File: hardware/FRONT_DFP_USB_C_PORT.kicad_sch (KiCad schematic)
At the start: 26 parts, among them J5 USB4200-03-A (VIRT FLAG MOUNT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, Q18 PMOS, Q19 PMOS, Q20 PMOS, Q21 PMOS

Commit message: finnished rudimentry schimatics still needs alot of work
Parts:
- removed D11 (x2): ~, symbol CARTHING:PUSB3FR6
- removed U12: ~, symbol CARTHING:USB5916C
- added D11 (x2): ~, symbol CARTHING:PUSB3FR6
- added U12: ~, symbol CARTHING:USB5916C
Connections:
- net +3V3: no longer U14.14 (SLV_ADDR)
- net GND: now also U14.14 (SLV_ADDR), D11.2 (GND), D11.2 (GND)
- net B_USB-C_BUCK_OUT renamed F_USB-C_BUCK_OUT
- net UFP_2_N renamed DFP_2_N
- net DFP_2_N: now also D11.3 (CH2), U12.7 (USB2DN_DM1/PRT_DIS_M1)
- net UFP_2_P renamed DFP_2_P
- net DFP_2_P: now also D11.1 (CH1), U12.6 (USB2DN_DP1/PRT_DIS_P1)
- net UFP_3_RXA_N renamed DFP_3_RXA_N
- net DFP_3_RXA_N: now also D11.7 (CH6), U12.12 (USB3DN_RXDM1A)
- net UFP_3_RXA_P renamed DFP_3_RXA_P
- net DFP_3_RXA_P: now also D11.6 (CH5), U12.11 (USB3DN_RXDP1A)
- net UFP_3_RXB_N renamed DFP_3_RXB_N
- net DFP_3_RXB_N: now also D11.4 (CH3), U12.19 (USB3DN_RXDM1B)
- net UFP_3_RXB_P renamed DFP_3_RXB_P
- net DFP_3_RXB_P: now also D11.5 (CH4), U12.18 (USB3DN_RXDP1B)
- net UFP_3_TXA_N renamed DFP_3_TXA_N
- net DFP_3_TXA_N: now also D11.5 (CH4)
- net UFP_3_TXA_P renamed DFP_3_TXA_P
- net DFP_3_TXA_P: now also D11.4 (CH3)
- net UFP_3_TXB_N renamed DFP_3_TXB_N
- net DFP_3_TXB_N: now also D11.1 (CH1), U12.16 (USB3DN_TXDM1B)
- net UFP_3_TXB_P renamed DFP_3_TXB_P
- net DFP_3_TXB_P: now also D11.3 (CH2), U12.15 (USB3DN_TXDP1B)
- net UFP_CC1 renamed DFP_CC1
- net DFP_CC1: now also D11.6 (CH5)
- net UFP_CC2 renamed DFP_CC2
- net DFP_CC2: now also D11.7 (CH6)
- net UFP_CC_CTRL renamed DFP_CC_CTRL
- net UFP_CC_ORIENT renamed DFP_CC_ORIENT
- net DFP_CC_ORIENT: now also U12.50 (AB1/ATTACHMUX1B/GPIO65)
- net UFP_PD_INT renamed DFP_PD_INT
- net UFP_VBUS renamed DFP_VBUS
- new net DFP_C_ATTACH_1: U12.76 (C_ATTACH1/ATTACHMUX1A/GPIO1)
- no-connect marks 4 -> 5
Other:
- note added: "ADDR 0XE0"
- note added: "PMPB27EP"
- note removed: "ADDR 0XE4"

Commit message: working on hardware
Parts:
- added C100 (x2), C99 (x2): 0.1uF, Capacitor_SMD:C_0603_1608Metric, symbol Device:C
- C80, C81, C82, C83, C84, C85: footprint (none) -> Capacitor_SMD:C_0603_1608Metric
- JP1, JP2, JP5, JP6, JP7: footprint (none) -> Jumper:SolderJumper-3_P1.3mm_Open_RoundedPad1.0x1.5mm_NumberLabels
- Q18, Q19, Q20, Q21: footprint (none) -> CARTHING:TRANS_PMPB11EN_115
- TP1: footprint (none) -> TestPoint:TestPoint_Pad_D1.5mm
- renumbered U12 to U13
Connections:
- net DFP_3_RXB_N: now also C99.2; no longer J5.B10 (RX1-)
- net DFP_3_RXB_P: now also C100.1; no longer J5.B11 (RX1+)
- net DFP_3_TXB_N: now also C99.2; no longer J5.B3 (TX2-)
- net DFP_3_TXB_P: now also C100.1; no longer J5.B2 (TX2+)
- new net: C100.2, J5.B11 (RX1+)
- new net: C99.1, J5.B10 (RX1-)
- new net: C100.2, J5.B2 (TX2+)
- new net: C99.1, J5.B3 (TX2-)
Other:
- note added: "EHUB CHIP DFP BLOCK"
- note added: "ESD PROTECTION"
- note added: "FRONT USB-C PORT CONTROLER"
- note added: "PHISICAL USB-C DOWNSTREAM PORT"
- moved on the sheet: C80, C81, C82, C83, C84, C85, D11, JP1, JP2, JP5, JP6, JP7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

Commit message: working assighning footprints still
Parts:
- R89, R90, R91, R92, R93: footprint (none) -> Resistor_SMD:R_0603_1608Metric
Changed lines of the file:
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@@
       (effects (font (size 1.27 1.27)) (justify left))
     )
-    (property "Footprint" "" (at 193.802 144.78 90)
+    (property "Footprint" "Resistor_SMD:R_0603_1608Metric" (at 193.802 144.78 90)
       (effects (font (size 1.27 1.27)) hide)
     )
@@
       (effects (font (size 1.27 1.27)))
     )
-    (property "Footprint" "" (at 177.8 128.778 90)
+    (property "Footprint" "Resistor_SMD:R_0603_1608Metric" (at 177.8 128.778 90)
       (effects (font (size 1.27 1.27)) hide)
     )
@@
       (effects (font (size 1.27 1.27)) (justify left))
     )
-    (property "Footprint" "" (at 73.152 170.18 90)
+    (property "Footprint" "Resistor_SMD:R_0603_1608Metric" (at 73.152 170.18 90)
       (effects (font (size 1.27 1.27)) hide)
     )
@@
       (effects (font (size 1.27 1.27)))
     )
-    (property "Footprint" "" (at 177.8 154.178 90)
+    (property "Footprint" "Resistor_SMD:R_0603_1608Metric" (at 177.8 154.178 90)
       (effects (font (size 1.27 1.27)) hide)
     )
@@
       (effects (font (size 1.27 1.27)) (justify left))
     )
-    (property "Footprint" "" (at 193.802 119.38 90)
-      (effects (font (size 1.27 1.27)) hide)
-    )
+    (property "Footprint" "Resistor_SMD:R_0603_1608Metric" (at 193.802 119.38 90)
+      (effects (font (size 1.27 1.27)) hide)
+    )

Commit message: FINALY starting the pcb
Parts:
- D11: footprint (none) -> CARTHING:PUSB3AB6Z_NEX
- J5: footprint (none) -> CARTHING:USB4200-03-A_REVA
- U13: footprint (none) -> CARTHING:VQFN100_KD_MCH
- U14: footprint (none) -> CARTHING:PTN5100BSMP
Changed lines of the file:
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@@
       (effects (font (size 1.27 1.27)))
     )
-    (property "Footprint" "" (at 44.45 54.61 0)
+    (property "Footprint" "CARTHING:USB4200-03-A_REVA" (at 44.45 54.61 0)
       (effects (font (size 1.27 1.27)) hide)
     )
@@
       (effects (font (size 1.27 1.27)))
     )
-    (property "Footprint" "" (at 138.43 25.4 0)
+    (property "Footprint" "CARTHING:PUSB3AB6Z_NEX" (at 138.43 25.4 0)
       (effects (font (size 1.27 1.27)) hide)
     )
@@
       (effects (font (size 1.27 1.27)))
     )
-    (property "Footprint" "" (at 241.3 87.63 0)
+    (property "Footprint" "CARTHING:VQFN100_KD_MCH" (at 241.3 87.63 0)
       (effects (font (size 1.27 1.27)) hide)
     )
@@
       (effects (font (size 1.27 1.27)))
     )
-    (property "Footprint" "" (at 138.43 53.34 0)
+    (property "Footprint" "CARTHING:PUSB3AB6Z_NEX" (at 138.43 53.34 0)
       (effects (font (size 1.27 1.27)) hide)
     )
@@
       (effects (font (size 1.27 1.27)))
     )
-    (property "Footprint" "" (at 102.87 127 0)
-      (effects (font (size 1.27 1.27)) hide)
-    )
+    (property "Footprint" "CARTHING:PTN5100BSMP" (at 102.87 127 0)
+      (effects (font (size 1.27 1.27)) hide)
+    )

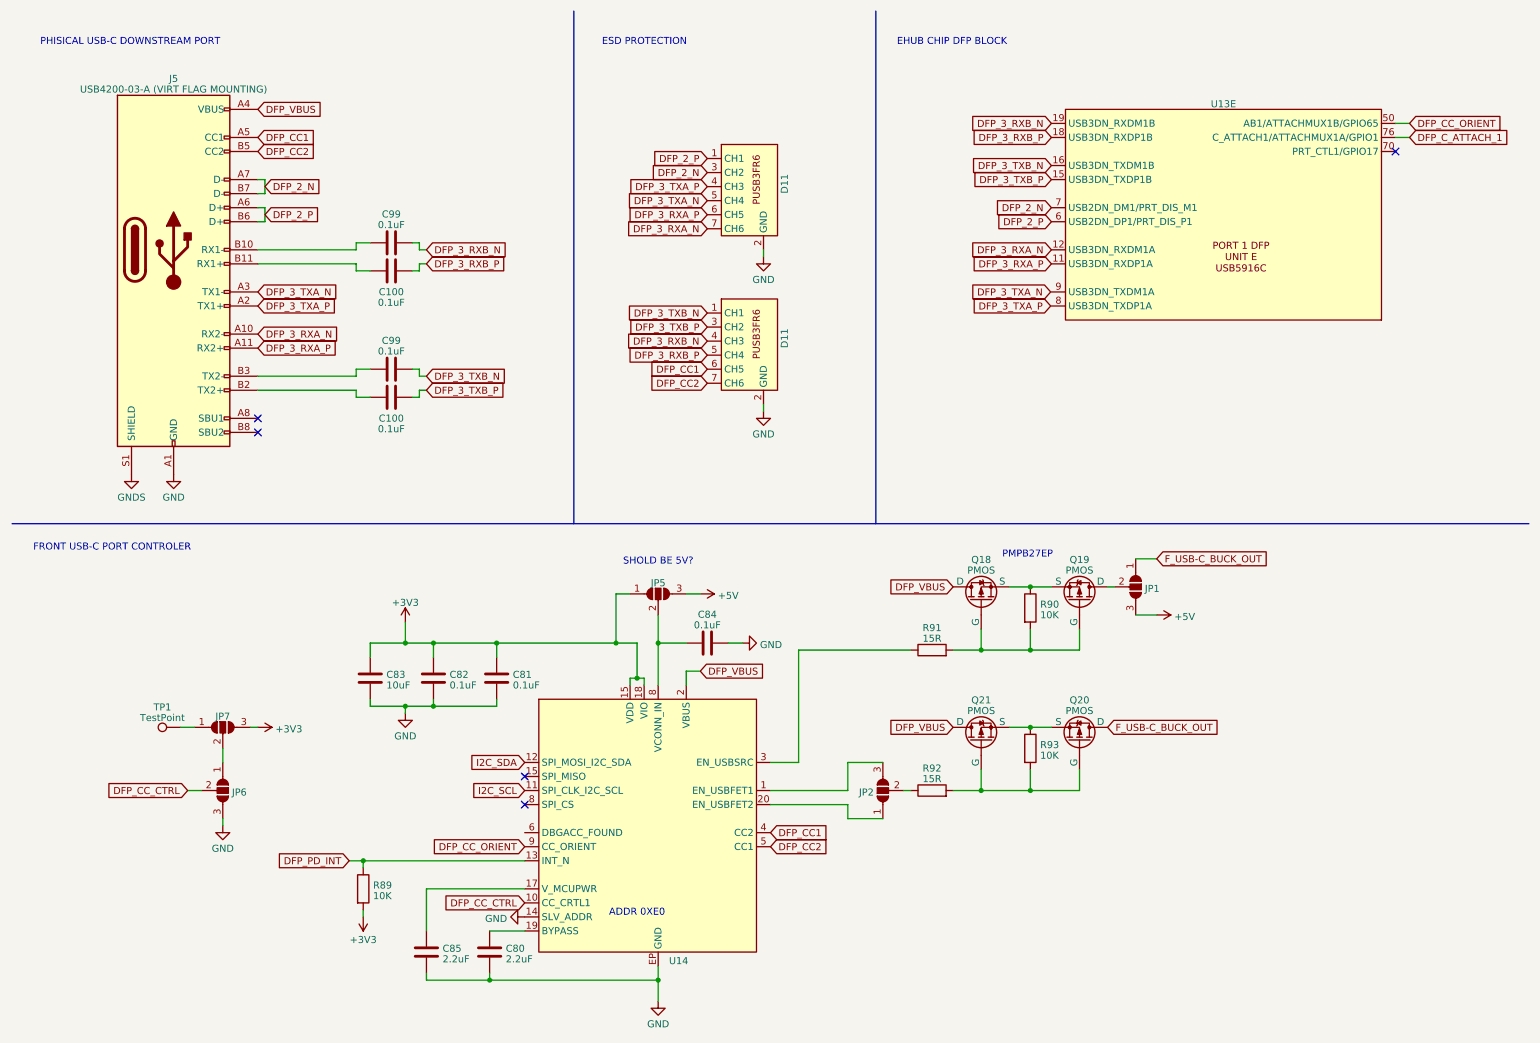
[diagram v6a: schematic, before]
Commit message: worked on usb port and display routing
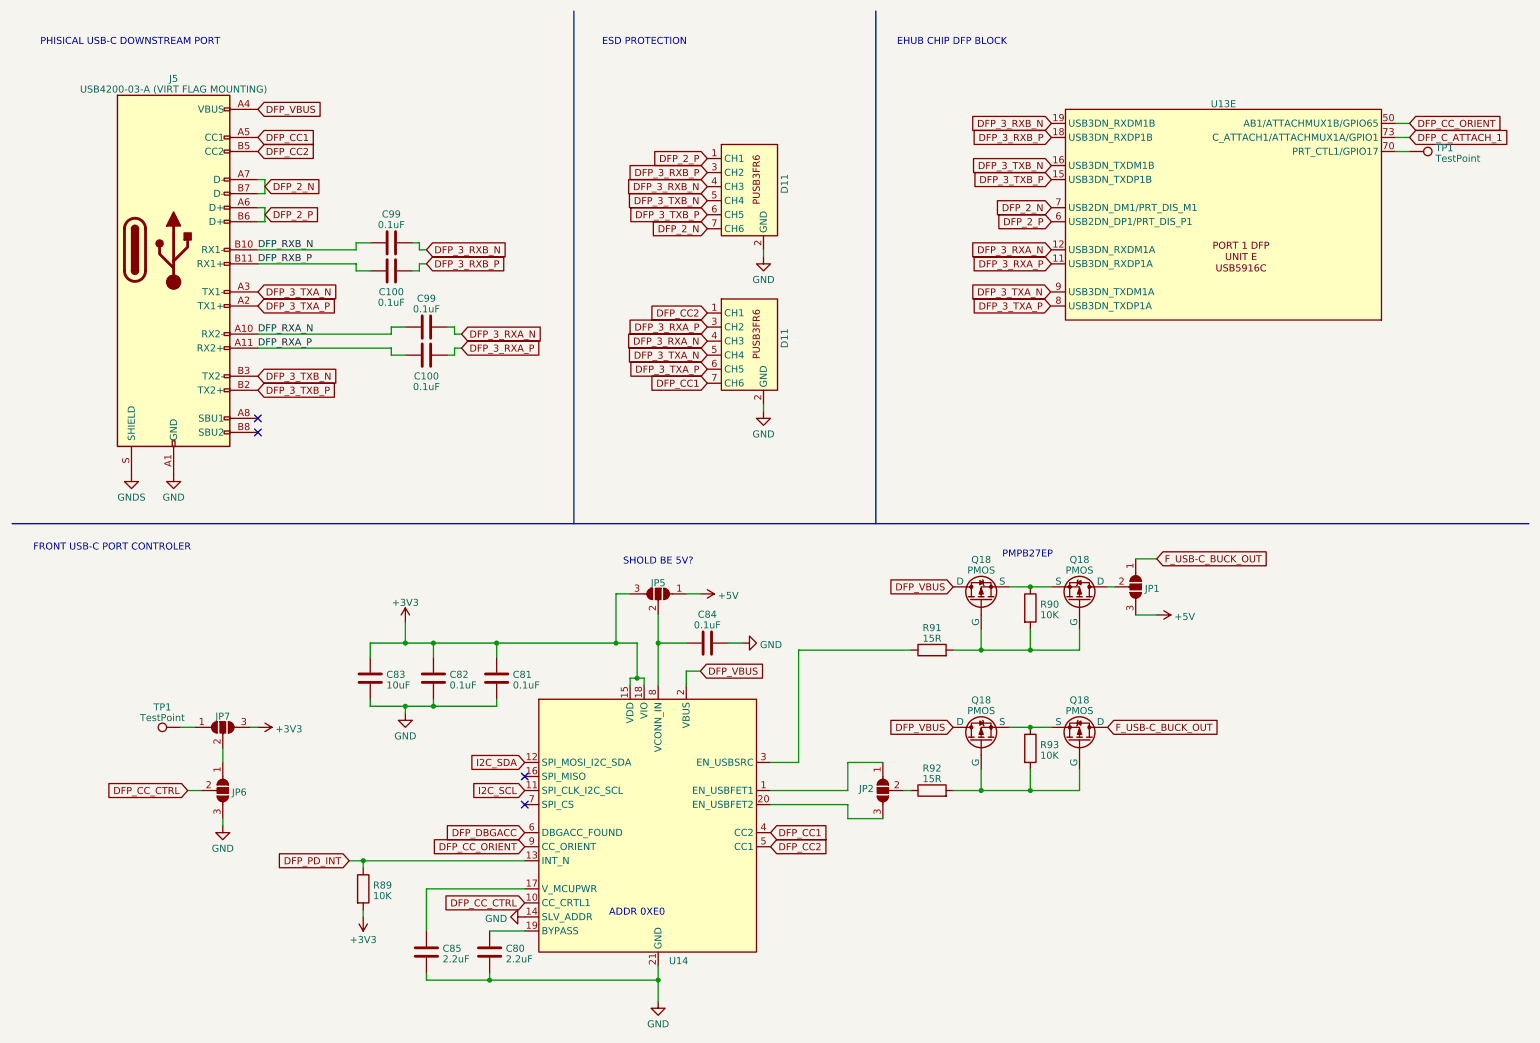
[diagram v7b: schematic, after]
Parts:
- removed Q19, Q20, Q21: PMOS, CARTHING:TRANS_PMPB11EN_115, symbol Simulation_SPICE:PMOS
- added Q18 (x3): PMOS, CARTHING:TRANS_PMPB11EN_115, symbol Simulation_SPICE:PMOS
- added TP1: TestPoint, TestPoint:TestPoint_Pad_D1.5mm, symbol Connector:TestPoint
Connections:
- net +3V3: now also JP5.3 (B); no longer JP5.1 (A)
- net +5V: now also JP5.1 (A); no longer JP5.3 (B)
- net DFP_2_N: now also D11.7 (CH6); no longer D11.3 (CH2)
- net DFP_3_RXA_N: now also C99.2, D11.4 (CH3); no longer D11.7 (CH6), J5.A10 (RX2-)
- net DFP_3_RXA_P: now also C100.1, D11.3 (CH2); no longer D11.6 (CH5), J5.A11 (RX2+)
- net DFP_3_RXB_N: now also D11.4 (CH3); no longer D11.4 (CH3)
- net DFP_3_RXB_P: now also D11.3 (CH2); no longer D11.5 (CH4)
- net DFP_3_TXA_N: now also D11.5 (CH4); no longer D11.5 (CH4)
- net DFP_3_TXA_P: now also D11.6 (CH5); no longer D11.4 (CH3)
- net DFP_3_TXB_N: now also D11.5 (CH4), J5.B3 (TX2-); no longer C99.2, D11.1 (CH1)
- net DFP_3_TXB_P: now also D11.6 (CH5), J5.B2 (TX2+); no longer C100.1, D11.3 (CH2)
- net DFP_CC1: now also D11.7 (CH6); no longer D11.6 (CH5)
- net DFP_CC2: now also D11.1 (CH1); no longer D11.7 (CH6)
- net DFP_C_ATTACH_1: now also U13.73 (C_ATTACH1/ATTACHMUX1A/GPIO1); no longer U13.76 (C_ATTACH1/ATTACHMUX1A/GPIO1)
- net DFP_VBUS: now also Q18.2 (D), Q18.5 (D), Q18.6 (D), Q18.7 (D), Q18.1 (D), Q18.2 (D), Q18.5 (D), Q18.6 (D), Q18.7 (D)
- net F_USB-C_BUCK_OUT: now also Q18.1 (D), Q18.2 (D), Q18.5 (D), Q18.6 (D), Q18.7 (D)
- net GND: now also U14.21 (GND); no longer U14.EP (GND)
- net GNDS: now also J5.S (SHIELD); no longer J5.S1 (SHIELD)
- net at R93.1: now also Q18.4 (S), Q18.4 (S), Q18.8 (S), Q18.8 (S)
- net at R92.2, R93.2: now also Q18.3 (G), Q18.3 (G)
- net at R90.2, R91.2: now also Q18.3 (G), Q18.3 (G); no longer Q18.2 (G)
- net at R90.1: now also Q18.4 (S), Q18.8 (S), Q18.4 (S), Q18.8 (S); no longer Q18.3 (S)
- net at JP2.1 (A): now also U14.1 (EN_USBFET1); no longer U14.20 (EN_USBFET2)
- net at JP2.3 (B): now also U14.20 (EN_USBFET2); no longer U14.1 (EN_USBFET1)
- net at JP1.2 (C): now also Q18.1 (D), Q18.2 (D), Q18.5 (D), Q18.6 (D), Q18.7 (D)
- net DFP_RXB_P: now reaches C100.2, J5.B11 (RX1+)
- net DFP_RXB_N: now reaches C99.1, J5.B10 (RX1-)
- net DFP_RXA_P: now reaches C100.2
- net DFP_RXA_P: now also J5.A11 (RX2+); no longer J5.B2 (TX2+)
- net DFP_RXA_N: now reaches C99.1
- net DFP_RXA_N: now also J5.A10 (RX2-); no longer J5.B3 (TX2-)
- net at U13.70 (PRT_CTL1/GPIO17): now also TP1.1
- net DFP_DBGACC: now reaches U14.6 (DBGACC_FOUND)
- no-connect marks 5 -> 4
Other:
- moved on the sheet: C100, C99

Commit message: working in final routing
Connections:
- net DFP_3_TXA_N: now also U13.9 (USB3DN_TXDM1A)
- net DFP_3_TXA_P: now also U13.8 (USB3DN_TXDP1A)
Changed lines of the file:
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@@
+    (stroke (width 0) (type default))
+  )
+  (wire (pts (xy 198.12 62.23) (xy 199.39 62.23))
     (stroke (width 0) (type default))
   )
@@
   )
   (wire (pts (xy 148.59 147.32) (xy 153.67 147.32))
+    (stroke (width 0) (type default))
+  )
+  (wire (pts (xy 198.12 64.77) (xy 199.39 64.77))
     (stroke (width 0) (type default))
   )
@@
     )
   )
-  (global_label "DFP_3_TXA_P" (shape input) (at 199.2512 64.77 180) (fields_autoplaced)
-    (effects (font (size 1.27 1.27)) (justify right))
-    (property "Intersheetrefs" "${INTERSHEET_REFS}" (at 184.0688 64.77 0)
+  (global_label "DFP_3_TXA_P" (shape input) (at 198.12 64.77 180) (fields_autoplaced)
+    (effects (font (size 1.27 1.27)) (justify right))
+    (property "Intersheetrefs" "${INTERSHEET_REFS}" (at 182.9376 64.77 0)
       (effects (font (size 1.27 1.27)) (justify right) hide)
     )
@@
     )
   )
-  (global_label "DFP_3_TXA_N" (shape input) (at 199.2512 62.23 180) (fields_autoplaced)
-    (effects (font (size 1.27 1.27)) (justify right))
-    (property "Intersheetrefs" "${INTERSHEET_REFS}" (at 184.0083 62.23 0)
+  (global_label "DFP_3_TXA_N" (shape input) (at 198.12 62.23 180) (fields_autoplaced)
+    (effects (font (size 1.27 1.27)) (justify right))
+    (property "Intersheetrefs" "${INTERSHEET_REFS}" (at 182.8771 62.23 0)
       (effects (font (size 1.27 1.27)) (justify right) hide)
     )
@@
     (pin "3")
     (pin "4")
-    (pin "8")
     (pin "5")
     (pin "6")
     (pin "7")
+    (pin "8")
     (instances
       (project "usbc-car-module"
@@
   (symbol (lib_id "CARTHING:USB5916C") (at 233.68 55.88 180) (unit 5)
     (in_bom yes) (on_board yes) (dnp no) (fields_autoplaced)
-    (property "Reference" "U13" (at 230.505 28.2481 0)
+    (property "Reference" "U13" (at 234.95 68.2719 0)
       (effects (font (size 1.27 1.27)))
     )
@@
     )
     (pin "10")
+    (pin "101")
     (pin "17")
     (pin "2")
@@
     (pin "93")
     (pin "98")
-    (pin "EP")
     (pin "1")
     (pin "20")
@@
           (reference "U13") (unit 5)
         )
+        (path "/fae025e9-99c5-40c1-af6f-99dc1edbfa43/7a7a6512-c96f-448a-bb8d-4d6e185adf7f"
+          (reference "U13") (unit 5)
+        )
